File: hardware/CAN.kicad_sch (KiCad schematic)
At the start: 10 parts, among them IC2 TCAN3413DR, J11 CarCANConnector

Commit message: cleanup and label fixes
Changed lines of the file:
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@@
 	)
 	(hierarchical_label "LV_GND"
-		(shape input)
+		(shape passive)
 		(at 179.07 80.01 0)
 		(effects
@@
 	)
 	(hierarchical_label "{CAN}"
-		(shape input)
+		(shape bidirectional)
 		(at 137.16 67.31 0)
 		(effects

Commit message: major clean ups, fix LV enable labels, fixes and cleanup
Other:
- moved on the sheet: J11
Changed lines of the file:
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@@
 	(wire
 		(pts
-			(xy 215.9 118.11) (xy 222.25 118.11)
+			(xy 199.39 118.11) (xy 205.74 118.11)
 		)
 		(stroke
@@
 	(wire
 		(pts
-			(xy 215.9 123.19) (xy 222.25 123.19)
+			(xy 199.39 123.19) (xy 205.74 123.19)
 		)
 		(stroke
@@
 	)
 	(label "CANH"
-		(at 215.9 118.11 0)
+		(at 199.39 118.11 0)
 		(effects
 			(font
@@
 	)
 	(label "CANL"
-		(at 215.9 123.19 0)
+		(at 199.39 123.19 0)
 		(effects
 			(font
@@
 	(symbol
 		(lib_id "utsvt_connectors:CarCANConnector")
-		(at 231.14 120.65 0)
+		(at 214.63 120.65 0)
 		(mirror y)
 		(unit 1)
@@
 		(fields_autoplaced yes)
 		(property "Reference" "J11"
-			(at 231.14 111.76 0)
+			(at 214.63 111.76 0)
 			(show_name no)
 			(do_not_autoplace no)
@@
 		)
 		(property "Value" "CarCANConnector"
-			(at 231.14 114.3 0)
+			(at 214.63 114.3 0)
 			(show_name no)
 			(do_not_autoplace no)
@@
 		)
 		(property "Footprint" "UTSVT_Connectors:Molex_Nano-Fit_105309-xx02_1x02_P2.50mm_Vertical"
-			(at 231.14 129.54 0)
+			(at 214.63 129.54 0)
 			(hide yes)
 			(show_name no)
@@
 		)
 		(property "Datasheet" "https://www.digikey.com/en/products/detail/molex/1053091102/7693146"
-			(at 227.33 113.03 0)
+			(at 210.82 113.03 0)
 			(hide yes)
 			(show_name no)
@@
 		)
 		(property "Description" "Connector"
-			(at 231.14 120.65 0)
+			(at 214.63 120.65 0)
 			(hide yes)
 			(show_name no)
@@
 		)
 		(property "P/N" "1053091102"
-			(at 231.14 120.65 0)
+			(at 214.63 120.65 0)
 			(hide yes)
 			(show_name no)
@@
 		)
 		(property "Assemble" "N"
-			(at 231.14 120.65 0)
-			(hide yes)
-			(show_name no)
+			(at 214.63 120.65 0)
+			(hide yes)
+			(show_name no)

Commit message: nearly all reviews addressed yippeeeeee
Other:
- moved on the sheet: C40, C42, C43, C44, D5, IC2, J11, JP1, R55, R56

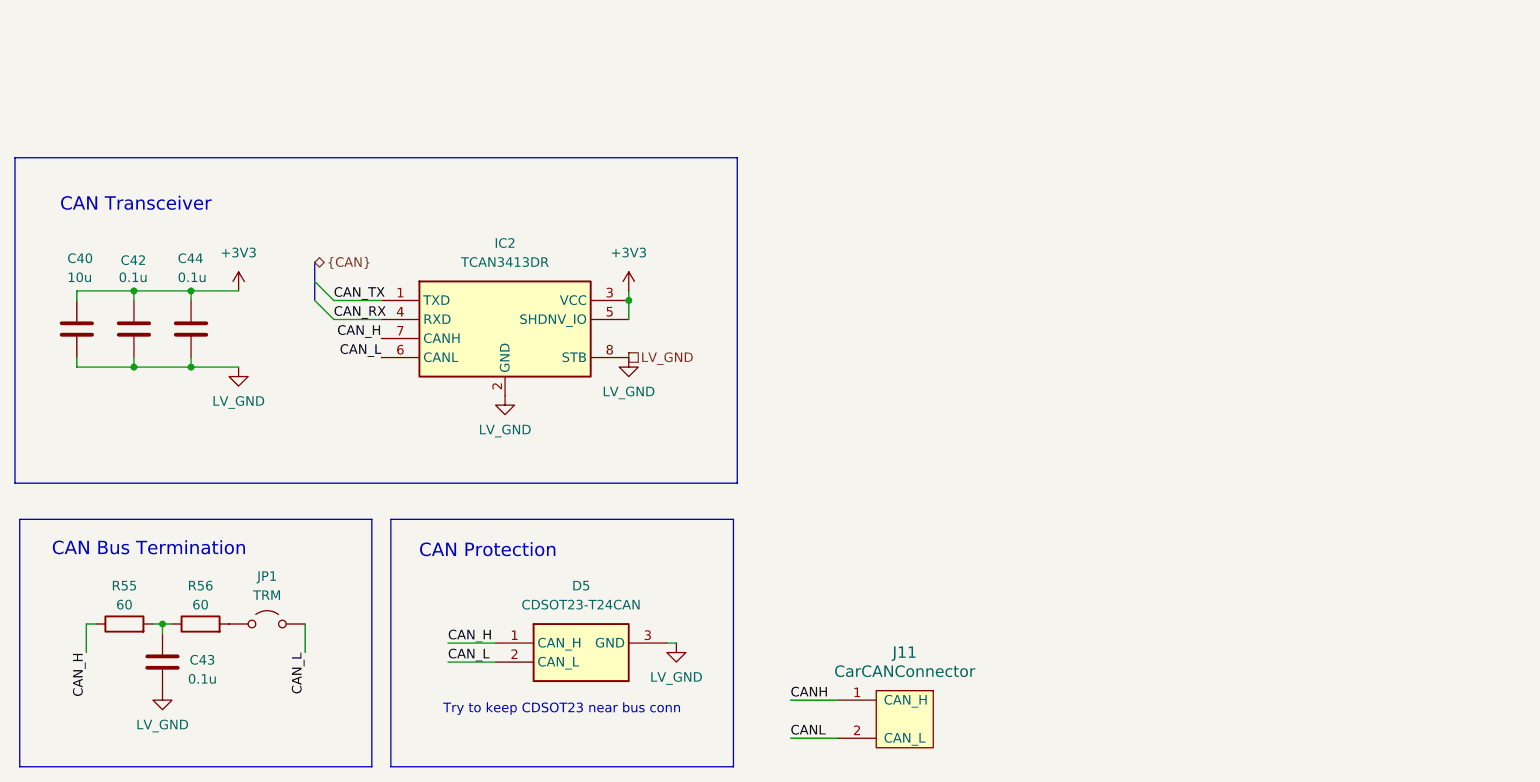
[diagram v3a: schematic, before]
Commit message: done all obbb specific reviews beside indicator led resistor values + math, goodnight
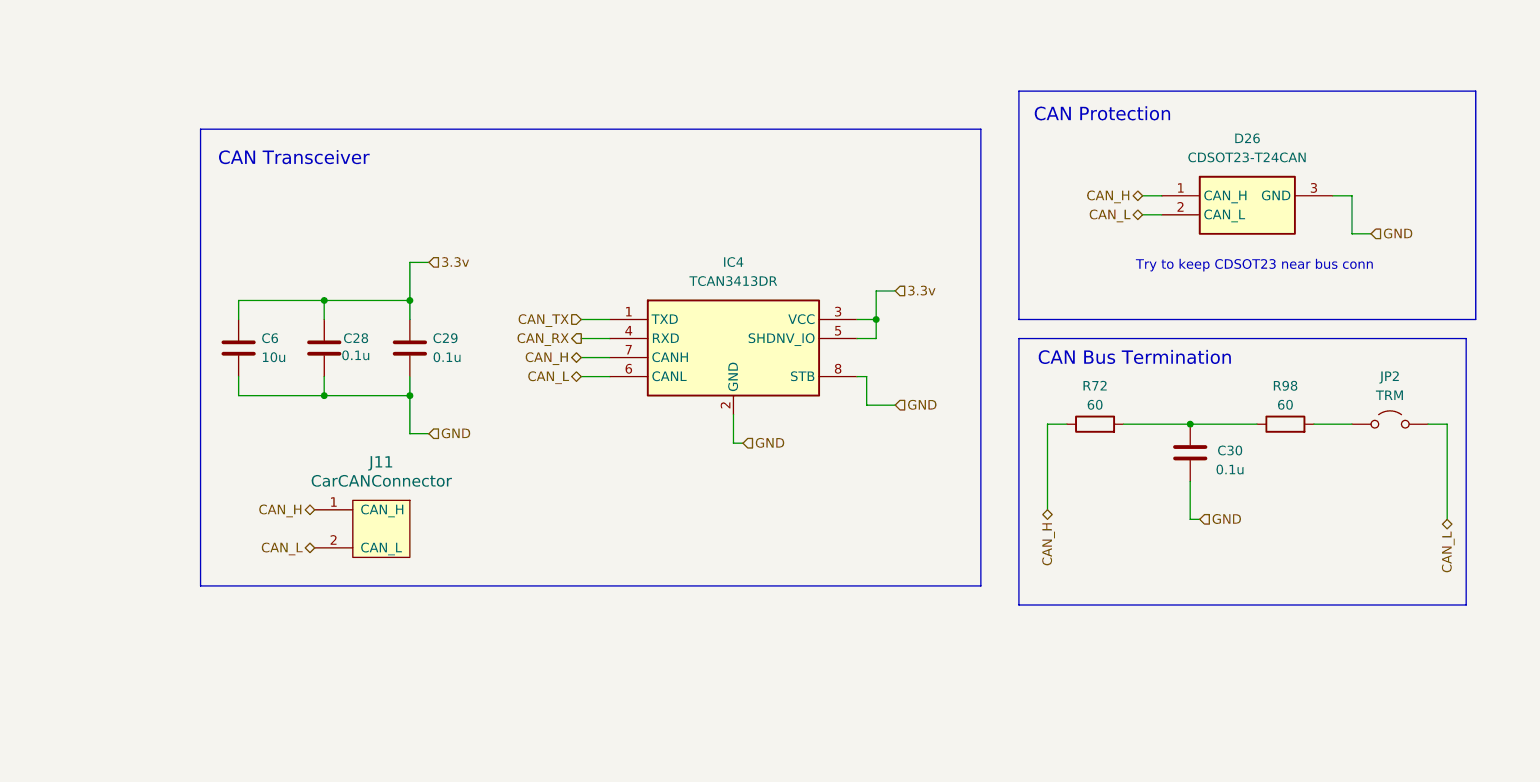
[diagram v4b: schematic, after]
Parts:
- removed C40: 10u, Capacitor_SMD:C_0805_2012Metric_Pad1.18x1.45mm_HandSolder, symbol Device:C
- removed C42, C44: 0.1u, Capacitor_SMD:C_0603_1608Metric_Pad1.08x0.95mm_HandSolder, symbol Device:C
- removed C43: 0.1u, Capacitor_SMD:C_0603_1608Metric_Pad1.08x0.95mm_HandSolder, symbol ECE319K:C
- removed D5: CDSOT23-T24CAN, LHRS_Passives:CDSOT23-T24CAN, symbol CDSOT23-T24CAN:CDSOT23-T24CAN
- removed IC2: TCAN3413DR, LHRS_Passives:TCAN3413DR, symbol TCAN3413DR:TCAN3413DR
- removed JP1: TRM, Connector_PinHeader_2.54mm:PinHeader_1x02_P2.54mm_Vertical, symbol Jumper:Jumper_2_Open
- removed R55, R56: 60, Resistor_SMD:R_0603_1608Metric_Pad0.98x0.95mm_HandSolder, symbol Device:R
- added C28, C29: 0.1u, Capacitor_SMD:C_0603_1608Metric_Pad1.08x0.95mm_HandSolder, symbol Device:C
- added C30: 0.1u, Capacitor_SMD:C_0603_1608Metric_Pad1.08x0.95mm_HandSolder, symbol ECE319K:C
- added C6: 10u, Capacitor_SMD:C_0805_2012Metric_Pad1.18x1.45mm_HandSolder, symbol Device:C
- added D26: CDSOT23-T24CAN, LHRS_Passives:CDSOT23-T24CAN, symbol CDSOT23-T24CAN:CDSOT23-T24CAN
- added IC4: TCAN3413DR, LHRS_Passives:TCAN3413DR, symbol TCAN3413DR:TCAN3413DR
- added JP2: TRM, Connector_PinHeader_2.54mm:PinHeader_1x02_P2.54mm_Vertical, symbol Jumper:Jumper_2_Open
- added R72, R98: 60, Resistor_SMD:R_0603_1608Metric_Pad0.98x0.95mm_HandSolder, symbol Device:R
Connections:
- net CANH is gone; now on net CAN_H: J11.1 (CAN_H)
- net CANL is gone; now on net CAN_L: J11.2 (CAN_L)
- net CAN_H: now also D26.1 (CAN_H), IC4.7 (CANH), R72.1
- net CAN_L: now also D26.2 (CAN_L), IC4.6 (CANL), JP2.2 (B)
- net CAN_RX: now also IC4.4 (RXD)
- net CAN_TX: now also IC4.1 (TXD)
- new net: C30.2, R72.2, R98.1
- new net: JP2.1 (A), R98.2
- new net 3.3v: C28.1, C29.1, C6.1, IC4.3 (VCC), IC4.5 (SHDNV_IO)
- new net GND: C28.2, C29.2, C30.1, C6.2, D26.3 (GND), IC4.2 (GND), IC4.8 (STB)
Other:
- moved on the sheet: J11

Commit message: fixes only thing left is finish assigning footprints, its frozen
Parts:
- C49: renamed from C6; Mouser P/N (none) -> GRM21BR61H106KE43K
- C50: renamed from C28; Mouser P/N (none) -> MLASH168SB7104KTNA01
- C51: renamed from C29; Mouser P/N (none) -> MLASH168SB7104KTNA01
- C52: renamed from C30; Mouser P/N (none) -> MLASH168SB7104KTNA01
- renumbered D26 to D28, IC4 to IC3, JP2 to JP1, R72 to R93, R98 to R94
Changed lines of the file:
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@@
 		(in_pos_files yes)
 		(dnp no)
-		(property "Reference" "C28"
+		(property "Reference" "C50"
 			(at 85.09 96.52 0)
 			(show_name no)
@@
 		)
 		(property "P/N" "MLASH168SB7104KTNA01"
+			(at 82.55 97.79 0)
+			(hide yes)
+			(show_name no)
+			(do_not_autoplace no)
+			(effects
+				(font
+					(size 1.27 1.27)
+				)
+			)
+		)
+		(property "Mouser P/N" "MLASH168SB7104KTNA01"
 			(at 82.55 97.79 0)
 			(hide yes)
@@
 			(project "PS-LVCarrier"
 				(path "/9bab2d9d-20f3-40ef-8545-e1299efec47e/f0804b6d-ee3f-4784-b794-2afd95f68c58"
-					(reference "C28")
+					(reference "C50")
 					(unit 1)
 				)
@@
 		(in_pos_files yes)
 		(dnp no)
-		(property "Reference" "C30"
+		(property "Reference" "C52"
 			(at 203.454 111.506 0)
 			(show_name no)
@@
 		)
 		(property "P/N" "MLASH168SB7104KTNA01"
+			(at 198.12 111.76 0)
+			(hide yes)
+			(show_name no)
+			(do_not_autoplace no)
+			(effects
+				(font
+					(size 1.27 1.27)
+				)
+			)
+		)
+		(property "Mouser P/N" "MLASH168SB7104KTNA01"
 			(at 198.12 111.76 0)
 			(hide yes)
@@
 			(project "PS-LVCarrier"
 				(path "/9bab2d9d-20f3-40ef-8545-e1299efec47e/f0804b6d-ee3f-4784-b794-2afd95f68c58"
-					(reference "C30")
+					(reference "C52")
 					(unit 1)
 				)
@@
 		(dnp no)
 		(fields_autoplaced yes)
-		(property "Reference" "JP2"
+		(property "Reference" "JP1"
 			(at 224.79 101.6 0)
 			(show_name no)
@@
 			(project "PS-LVCarrier"
 				(path "/9bab2d9d-20f3-40ef-8545-e1299efec47e/f0804b6d-ee3f-4784-b794-2afd95f68c58"
-					(reference "JP2")
+					(reference "JP1")
 					(unit 1)
 				)
@@
 		(in_pos_files yes)
 		(dnp no)
-		(property "Reference" "C29"
+		(property "Reference" "C51"
 			(at 97.028 96.52 0)
 			(show_name no)
@@
 		)
 		(property "P/N" "MLASH168SB7104KTNA01"
+			(at 93.98 97.79 0)
+			(hide yes)
+			(show_name no)
+			(do_not_autoplace no)
+			(effects
+				(font
+					(size 1.27 1.27)
+				)
+			)
+		)
+		(property "Mouser P/N" "MLASH168SB7104KTNA01"
 			(at 93.98 97.79 0)
 			(hide yes)
@@
 			(project "PS-LVCarrier"
 				(path "/9bab2d9d-20f3-40ef-8545-e1299efec47e/f0804b6d-ee3f-4784-b794-2afd95f68c58"
-					(reference "C29")
+					(reference "C51")
 					(unit 1)
 				)
@@
 		(in_pos_files yes)
 		(dnp no)
-		(property "Reference" "C6"
+		(property "Reference" "C49"
 			(at 74.168 96.52 0)
 			(show_name no)
@@
 		)
 		(property "P/N" "GRM21BR61H106KE43K"
+			(at 71.12 97.79 0)
+			(hide yes)
+			(show_name no)
+			(do_not_autoplace no)
+			(effects
+				(font
+					(size 1.27 1.27)
+				)
+			)
+		)
+		(property "Mouser P/N" "GRM21BR61H106KE43K"
 			(at 71.12 97.79 0)
 			(hide yes)
@@
 			(project "PS-LVCarrier"
 				(path "/9bab2d9d-20f3-40ef-8545-e1299efec47e/f0804b6d-ee3f-4784-b794-2afd95f68c58"
-					(reference "C6")
+					(reference "C49")
 					(unit 1)
 				)
@@
 		(in_pos_files yes)
 		(dnp no)
-		(property "Reference" "R98"
+		(property "Reference" "R94"
 			(at 210.82 102.87 90)
 			(show_name no)
@@
 			(project "PS-LVCarrier"
 				(path "/9bab2d9d-20f3-40ef-8545-e1299efec47e/f0804b6d-ee3f-4784-b794-2afd95f68c58"
-					(reference "R98")
+					(reference "R94")
 					(unit 1)
 				)
@@
 		(dnp no)
 		(fields_autoplaced yes)
-		(property "Reference" "D26"
+		(property "Reference" "D28"
 			(at 205.74 69.85 0)
 			(show_name no)
@@
 			(project "PS-LVCarrier"
 				(path "/9bab2d9d-20f3-40ef-8545-e1299efec47e/f0804b6d-ee3f-4784-b794-2afd95f68c58"
-					(reference "D26")
+					(reference "D28")
 					(unit 1)
 				)
@@
 		(dnp no)
 		(fields_autoplaced yes)
-		(property "Reference" "IC4"
+		(property "Reference" "IC3"
 			(at 137.16 86.36 0)
 			(show_name no)
@@
 			(project "PS-LVCarrier"
 				(path "/9bab2d9d-20f3-40ef-8545-e1299efec47e/f0804b6d-ee3f-4784-b794-2afd95f68c58"
-					(reference "IC4")
+					(reference "IC3")
 					(unit 1)
 				)
@@
 		(in_pos_files yes)
 		(dnp no)
-		(property "Reference" "R72"
+		(property "Reference" "R93"
 			(at 185.42 102.87 90)
 			(show_name no)
@@
 			(project "PS-LVCarrier"
 				(path "/9bab2d9d-20f3-40ef-8545-e1299efec47e/f0804b6d-ee3f-4784-b794-2afd95f68c58"
-					(reference "R72")
-					(unit 1)
-				)
+					(reference "R93")
+					(unit 1)
+				)

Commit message: switch branch
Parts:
- renumbered C49 to C57, C50 to C58, C51 to C59, C52 to C60, R93 to R98, R94 to R99
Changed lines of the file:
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@@
 		(in_pos_files yes)
 		(dnp no)
-		(property "Reference" "C50"
+		(property "Reference" "C58"
 			(at 85.09 96.52 0)
 			(show_name no)
@@
 			(project "PS-LVCarrier"
 				(path "/9bab2d9d-20f3-40ef-8545-e1299efec47e/f0804b6d-ee3f-4784-b794-2afd95f68c58"
-					(reference "C50")
+					(reference "C58")
 					(unit 1)
 				)
@@
 		(in_pos_files yes)
 		(dnp no)
-		(property "Reference" "C52"
+		(property "Reference" "C60"
 			(at 203.454 111.506 0)
 			(show_name no)
@@
 			(project "PS-LVCarrier"
 				(path "/9bab2d9d-20f3-40ef-8545-e1299efec47e/f0804b6d-ee3f-4784-b794-2afd95f68c58"
-					(reference "C52")
+					(reference "C60")
 					(unit 1)
 				)
@@
 		(in_pos_files yes)
 		(dnp no)
-		(property "Reference" "C51"
+		(property "Reference" "C59"
 			(at 97.028 96.52 0)
 			(show_name no)
@@
 			(project "PS-LVCarrier"
 				(path "/9bab2d9d-20f3-40ef-8545-e1299efec47e/f0804b6d-ee3f-4784-b794-2afd95f68c58"
-					(reference "C51")
+					(reference "C59")
 					(unit 1)
 				)
@@
 		(in_pos_files yes)
 		(dnp no)
-		(property "Reference" "C49"
+		(property "Reference" "C57"
 			(at 74.168 96.52 0)
 			(show_name no)
@@
 			(project "PS-LVCarrier"
 				(path "/9bab2d9d-20f3-40ef-8545-e1299efec47e/f0804b6d-ee3f-4784-b794-2afd95f68c58"
-					(reference "C49")
+					(reference "C57")
 					(unit 1)
 				)
@@
 		(in_pos_files yes)
 		(dnp no)
-		(property "Reference" "R94"
+		(property "Reference" "R99"
 			(at 210.82 102.87 90)
 			(show_name no)
@@
 			(project "PS-LVCarrier"
 				(path "/9bab2d9d-20f3-40ef-8545-e1299efec47e/f0804b6d-ee3f-4784-b794-2afd95f68c58"
-					(reference "R94")
+					(reference "R99")
 					(unit 1)
 				)
@@
 		(in_pos_files yes)
 		(dnp no)
-		(property "Reference" "R93"
+		(property "Reference" "R98"
 			(at 185.42 102.87 90)
 			(show_name no)
@@
 			(project "PS-LVCarrier"
 				(path "/9bab2d9d-20f3-40ef-8545-e1299efec47e/f0804b6d-ee3f-4784-b794-2afd95f68c58"
-					(reference "R93")
-					(unit 1)
-				)
+					(reference "R98")
+					(unit 1)
+				)

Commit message: review ts
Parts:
- renumbered C57 to C4, C58 to C5, C59 to C6, C60 to C7, D28 to D4, IC3 to IC1, J11 to J6, R98 to R15, R99 to R16
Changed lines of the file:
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@@
 		(in_pos_files yes)
 		(dnp no)
-		(property "Reference" "C58"
+		(property "Reference" "C5"
 			(at 85.09 96.52 0)
 			(show_name no)
@@
 			(project "PS-LVCarrier"
 				(path "/9bab2d9d-20f3-40ef-8545-e1299efec47e/f0804b6d-ee3f-4784-b794-2afd95f68c58"
-					(reference "C58")
+					(reference "C5")
 					(unit 1)
 				)
@@
 		(in_pos_files yes)
 		(dnp no)
-		(property "Reference" "C60"
+		(property "Reference" "C7"
 			(at 203.454 111.506 0)
 			(show_name no)
@@
 			(project "PS-LVCarrier"
 				(path "/9bab2d9d-20f3-40ef-8545-e1299efec47e/f0804b6d-ee3f-4784-b794-2afd95f68c58"
-					(reference "C60")
+					(reference "C7")
 					(unit 1)
 				)
@@
 		(dnp no)
 		(fields_autoplaced yes)
-		(property "Reference" "J11"
+		(property "Reference" "J6"
 			(at 90.17 113.03 0)
 			(show_name no)
@@
 			(project "PS-LVCarrier"
 				(path "/9bab2d9d-20f3-40ef-8545-e1299efec47e/f0804b6d-ee3f-4784-b794-2afd95f68c58"
-					(reference "J11")
+					(reference "J6")
 					(unit 1)
 				)
@@
 		(in_pos_files yes)
 		(dnp no)
-		(property "Reference" "C59"
+		(property "Reference" "C6"
 			(at 97.028 96.52 0)
 			(show_name no)
@@
 			(project "PS-LVCarrier"
 				(path "/9bab2d9d-20f3-40ef-8545-e1299efec47e/f0804b6d-ee3f-4784-b794-2afd95f68c58"
-					(reference "C59")
+					(reference "C6")
 					(unit 1)
 				)
@@
 		(in_pos_files yes)
 		(dnp no)
-		(property "Reference" "C57"
+		(property "Reference" "C4"
 			(at 74.168 96.52 0)
 			(show_name no)
@@
 			(project "PS-LVCarrier"
 				(path "/9bab2d9d-20f3-40ef-8545-e1299efec47e/f0804b6d-ee3f-4784-b794-2afd95f68c58"
-					(reference "C57")
+					(reference "C4")
 					(unit 1)
 				)
@@
 		(in_pos_files yes)
 		(dnp no)
-		(property "Reference" "R99"
+		(property "Reference" "R16"
 			(at 210.82 102.87 90)
 			(show_name no)
@@
 			(project "PS-LVCarrier"
 				(path "/9bab2d9d-20f3-40ef-8545-e1299efec47e/f0804b6d-ee3f-4784-b794-2afd95f68c58"
-					(reference "R99")
+					(reference "R16")
 					(unit 1)
 				)
@@
 		(dnp no)
 		(fields_autoplaced yes)
-		(property "Reference" "D28"
+		(property "Reference" "D4"
 			(at 205.74 69.85 0)
 			(show_name no)
@@
 			(project "PS-LVCarrier"
 				(path "/9bab2d9d-20f3-40ef-8545-e1299efec47e/f0804b6d-ee3f-4784-b794-2afd95f68c58"
-					(reference "D28")
+					(reference "D4")
 					(unit 1)
 				)
@@
 		(dnp no)
 		(fields_autoplaced yes)
-		(property "Reference" "IC3"
+		(property "Reference" "IC1"
 			(at 137.16 86.36 0)
 			(show_name no)
@@
 			(project "PS-LVCarrier"
 				(path "/9bab2d9d-20f3-40ef-8545-e1299efec47e/f0804b6d-ee3f-4784-b794-2afd95f68c58"
-					(reference "IC3")
+					(reference "IC1")
 					(unit 1)
 				)
@@
 		(in_pos_files yes)
 		(dnp no)
-		(property "Reference" "R98"
+		(property "Reference" "R15"
 			(at 185.42 102.87 90)
 			(show_name no)
@@
 			(project "PS-LVCarrier"
 				(path "/9bab2d9d-20f3-40ef-8545-e1299efec47e/f0804b6d-ee3f-4784-b794-2afd95f68c58"
-					(reference "R98")
-					(unit 1)
-				)
+					(reference "R15")
+					(unit 1)
+				)

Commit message: addressed
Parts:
- C4: Mouser P/N GRM21BR61H106KE43K -> (none)
- C5, C6, C7: Mouser P/N MLASH168SB7104KTNA01 -> (none)
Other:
- moved on the sheet: C4, C5, C6, C7, D4, IC1, J6, JP1, R15, R16
